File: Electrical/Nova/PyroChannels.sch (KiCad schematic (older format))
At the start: 2 parts

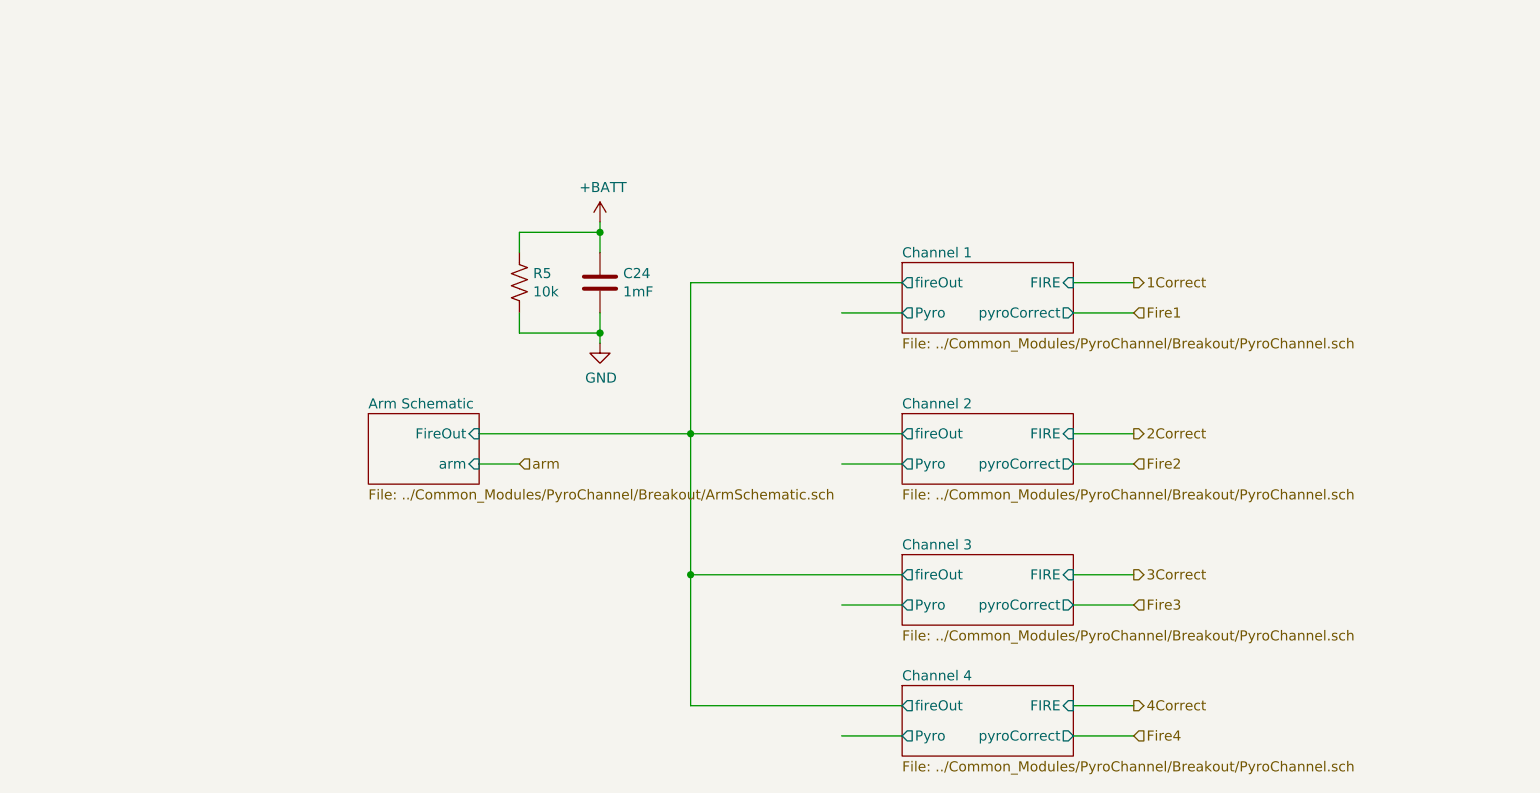
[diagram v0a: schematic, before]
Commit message: More Pin Additions for connectors and other misc.
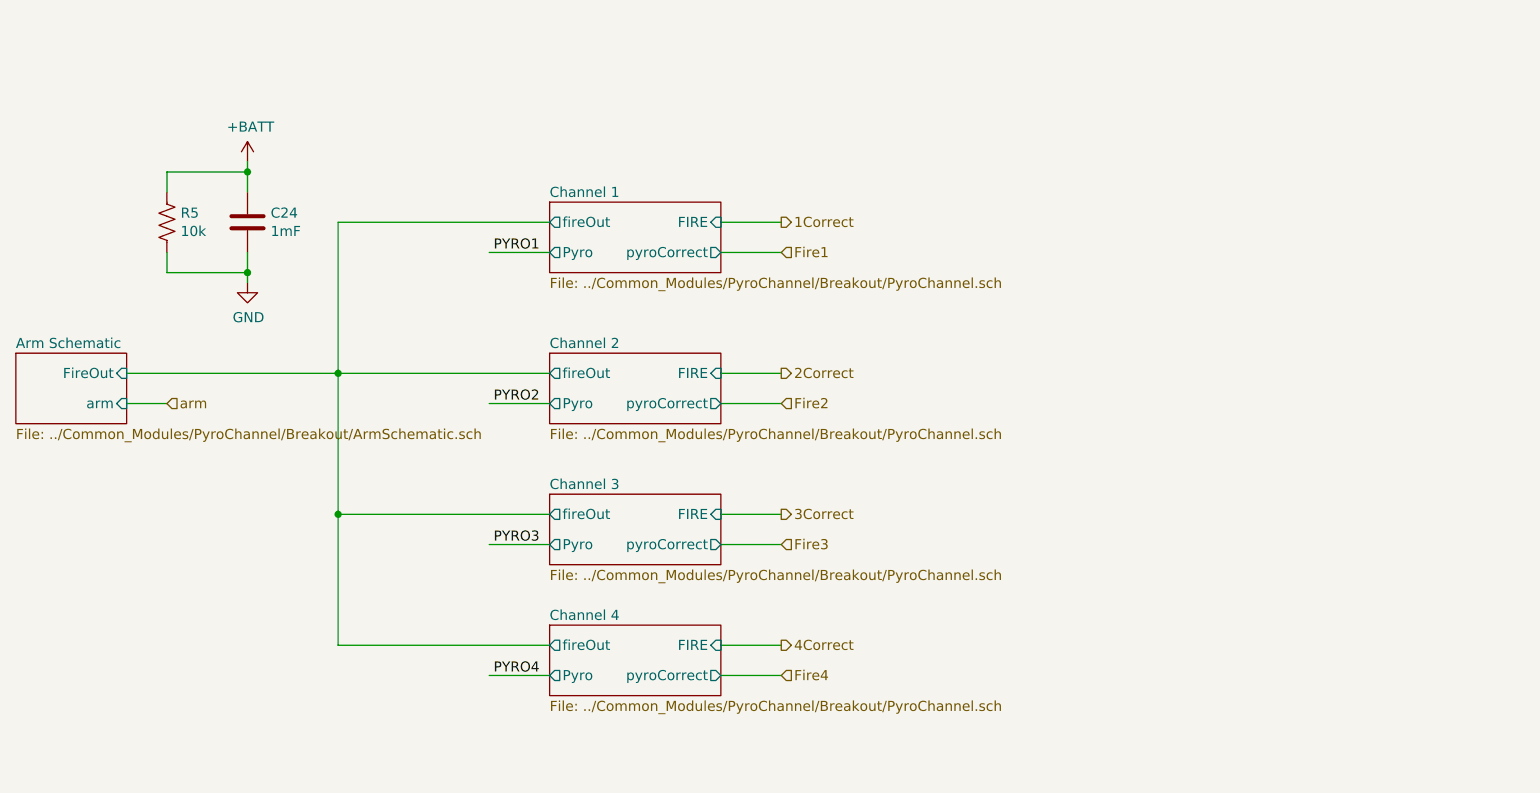
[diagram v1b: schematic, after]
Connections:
- net labels added: PYRO1, PYRO2, PYRO3, PYRO4
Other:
- moved on the sheet: C24, R5
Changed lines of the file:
@@
 $Descr USLetter 11000 8500
 encoding utf-8
-Sheet 12 21
+Sheet 10 21
 Title ""
 Date ""
@@
 L Device:C C24
 U 1 1 5F4497A2
-P 4450 3450
-F 0 "C24" H 4565 3496 50  0000 L CNN
-F 1 "1mF" H 4565 3405 50  0000 L CNN
-F 2 "" H 4488 3300 50  0001 C CNN
-F 3 "~" H 4450 3450 50  0001 C CNN
-F 4 "1189-3703-1-ND" H 4450 3450 50  0001 C CNN "digikey"
-	1    4450 3450
+P 2700 3150
+F 0 "C24" H 2815 3196 50  0000 L CNN
+F 1 "1mF" H 2815 3105 50  0000 L CNN
+F 2 "" H 2738 3000 50  0001 C CNN
+F 3 "~" H 2700 3150 50  0001 C CNN
+F 4 "1189-3703-1-ND" H 2700 3150 50  0001 C CNN "digikey"
+	1    2700 3150
 	1    0    0    -1
 $EndComp
@@
 L power:+BATT #PWR035
 U 1 1 5F449DDB
-P 4450 3150
-F 0 "#PWR035" H 4450 3000 50  0001 C CNN
-F 1 "+BATT" H 4465 3323 50  0000 C CNN
-F 2 "" H 4450 3150 50  0001 C CNN
-F 3 "" H 4450 3150 50  0001 C CNN
-	1    4450 3150
+P 2700 2850
+F 0 "#PWR035" H 2700 2700 50  0001 C CNN
+F 1 "+BATT" H 2715 3023 50  0000 C CNN
+F 2 "" H 2700 2850 50  0001 C CNN
+F 3 "" H 2700 2850 50  0001 C CNN
+	1    2700 2850
 	1    0    0    -1
 $EndComp
 Wire Wire Line
-	4450 3150 4450 3200
+	2700 2850 2700 2900
 $Comp
 L power:GND #PWR036
 U 1 1 5F44A4A7
-P 4450 3750
-F 0 "#PWR036" H 4450 3500 50  0001 C CNN
-F 1 "GND" H 4455 3577 50  0000 C CNN
-F 2 "" H 4450 3750 50  0001 C CNN
-F 3 "" H 4450 3750 50  0001 C CNN
-	1    4450 3750
+P 2700 3450
+F 0 "#PWR036" H 2700 3200 50  0001 C CNN
+F 1 "GND" H 2705 3277 50  0000 C CNN
+F 2 "" H 2700 3450 50  0001 C CNN
+F 3 "" H 2700 3450 50  0001 C CNN
+	1    2700 3450
 	1    0    0    -1
 $EndComp
 Wire Wire Line
-	4450 3600 4450 3700
+	2700 3300 2700 3400
 Wire Wire Line
-	4050 3600 4050 3700
+	2300 3300 2300 3400
 Wire Wire Line
-	4050 3700 4450 3700
-Connection ~ 4450 3700
+	2300 3400 2700 3400
+Connection ~ 2700 3400
 Wire Wire Line
-	4450 3700 4450 3750
+	2700 3400 2700 3450
 Wire Wire Line
-	4050 3300 4050 3200
+	2300 3000 2300 2900
 Wire Wire Line
-	4050 3200 4450 3200
-Connection ~ 4450 3200
+	2300 2900 2700 2900
+Connection ~ 2700 2900
 Wire Wire Line
-	4450 3200 4450 3300
+	2700 2900 2700 3000
 $Comp
 L Device:R_US R5
 U 1 1 5F6ECA83
-P 4050 3450
-F 0 "R5" H 4118 3496 50  0000 L CNN
-F 1 "10k" H 4118 3405 50  0000 L CNN
-F 2 "Resistor_SMD:R_0402_1005Metric" V 4090 3440 50  0001 C CNN
-F 3 "~" H 4050 3450 50  0001 C CNN
-	1    4050 3450
+P 2300 3150
+F 0 "R5" H 2368 3196 50  0000 L CNN
+F 1 "10k" H 2368 3105 50  0000 L CNN
+F 2 "Resistor_SMD:R_0402_1005Metric" V 2340 3140 50  0001 C CNN
+F 3 "~" H 2300 3150 50  0001 C CNN
+	1    2300 3150
 	1    0    0    -1
 $EndComp
-Text HLabel 7100 5050 2    50   Input ~ 0
+Text HLabel 5350 4750 2    50   Input ~ 0
 Fire3
-Text HLabel 7100 4900 2    50   Output ~ 0
+Text HLabel 5350 4600 2    50   Output ~ 0
 3Correct
 $Sheet
-S 5950 4800 850  350
+S 4200 4500 850  350
 U 5F71312E
 F0 "Channel 3" 50
 F1 "../Common_Modules/PyroChannel/Breakout/PyroChannel.sch" 50
-F2 "FIRE" I R 6800 4900 50
-F3 "pyroCorrect" O R 6800 5050 50
-F4 "fireOut" O L 5950 4900 50
-F5 "Pyro" O L 5950 5050 50
+F2 "FIRE" I R 5050 4600 50
+F3 "pyroCorrect" O R 5050 4750 50
+F4 "fireOut" O L 4200 4600 50
+F5 "Pyro" O L 4200 4750 50
 $EndSheet
 Wire Wire Line
-	7100 5050 6800 5050
+	5350 4750 5050 4750
 Wire Wire Line
-	6800 4900 7100 4900
+	5050 4600 5350 4600
 Wire Wire Line
-	5950 4200 4900 4200
+	4200 3900 3150 3900
 Wire Wire Line
-	5950 3450 4900 3450
+	4200 3150 3150 3150
 Wire Wire Line
-	4900 3450 4900 4200
-Connection ~ 4900 4200
+	3150 3150 3150 3900
+Connection ~ 3150 3900
 Wire Wire Line
-	4900 4200 3850 4200
+	3150 3900 2100 3900
 Wire Wire Line
-	4900 4200 4900 4900
+	3150 3900 3150 4600
 Wire Wire Line
-	4900 4900 5950 4900
-Text HLabel 4050 4350 2    50   Input ~ 0
+	3150 4600 4200 4600
+Text HLabel 2300 4050 2    50   Input ~ 0
 arm
 Wire Wire Line
-	3850 4350 4050 4350
-Text HLabel 7100 4200 2    50   Output ~ 0
+	2100 4050 2300 4050
+Text HLabel 5350 3900 2    50   Output ~ 0
 2Correct
-Text HLabel 7100 4350 2    50   Input ~ 0
+Text HLabel 5350 4050 2    50   Input ~ 0
 Fire2
 Wire Wire Line
-	7100 4350 6800 4350
+	5350 4050 5050 4050
 Wire Wire Line
-	7100 4200 6800 4200
+	5350 3900 5050 3900
 $Sheet
-S 5950 4100 850  350
+S 4200 3800 850  350
 U 5F449170
 F0 "Channel 2" 50
 F1 "../Common_Modules/PyroChannel/Breakout/PyroChannel.sch" 50
-F2 "FIRE" I R 6800 4200 50
-F3 "pyroCorrect" O R 6800 4350 50
-F4 "fireOut" O L 5950 4200 50
-F5 "Pyro" O L 5950 4350 50
+F2 "FIRE" I R 5050 3900 50
+F3 "pyroCorrect" O R 5050 4050 50
+F4 "fireOut" O L 4200 3900 50
+F5 "Pyro" O L 4200 4050 50
 $EndSheet
-Text HLabel 7100 3600 2    50   Input ~ 0
+Text HLabel 5350 3300 2    50   Input ~ 0
 Fire1
 Wire Wire Line
-	7100 3600 6800 3600
+	5350 3300 5050 3300
 Wire Wire Line
-	7100 3450 6800 3450
-Text HLabel 7100 3450 2    50   Output ~ 0
+	5350 3150 5050 3150
+Text HLabel 5350 3150 2    50   Output ~ 0
 1Correct
 $Sheet
-S 5950 3350 850  350
+S 4200 3050 850  350
 U 5F44909A
 F0 "Channel 1" 50
 F1 "../Common_Modules/PyroChannel/Breakout/PyroChannel.sch" 50
-F2 "FIRE" I R 6800 3450 50
-F3 "pyroCorrect" O R 6800 3600 50
-F4 "fireOut" O L 5950 3450 50
-F5 "Pyro" O L 5950 3600 50
+F2 "FIRE" I R 5050 3150 50
+F3 "pyroCorrect" O R 5050 3300 50
+F4 "fireOut" O L 4200 3150 50
+F5 "Pyro" O L 4200 3300 50
 $EndSheet
 Wire Wire Line
-	5950 3600 5650 3600
+	4200 3300 3900 3300
 Wire Wire Line
-	5950 4350 5650 4350
+	4200 4050 3900 4050
 Wire Wire Line
-	5950 5050 5650 5050
+	4200 4750 3900 4750
 $Sheet
-S 3300 4100 550  350
+S 1550 3800 550  350
 U 5F448D89
 F0 "Arm Schematic" 50
 F1 "../Common_Modules/PyroChannel/Breakout/ArmSchematic.sch" 50
-F2 "FireOut" I R 3850 4200 50
-F3 "arm" I R 3850 4350 50
+F2 "FireOut" I R 2100 3900 50
+F3 "arm" I R 2100 4050 50
 $EndSheet
-Text HLabel 7100 5700 2    50   Input ~ 0
+Text HLabel 5350 5400 2    50   Input ~ 0
 Fire4
 Wire Wire Line
-	7100 5700 6800 5700
+	5350 5400 5050 5400
 Wire Wire Line
-	7100 5550 6800 5550
-Text HLabel 7100 5550 2    50   Output ~ 0
+	5350 5250 5050 5250
+Text HLabel 5350 5250 2    50   Output ~ 0
 4Correct
 $Sheet
-S 5950 5450 850  350
+S 4200 5150 850  350
 U 6040FF20
 F0 "Channel 4" 50
 F1 "../Common_Modules/PyroChannel/Breakout/PyroChannel.sch" 50
-F2 "FIRE" I R 6800 5550 50
-F3 "pyroCorrect" O R 6800 5700 50
-F4 "fireOut" O L 5950 5550 50
-F5 "Pyro" O L 5950 5700 50
+F2 "FIRE" I R 5050 5250 50
+F3 "pyroCorrect" O R 5050 5400 50
+F4 "fireOut" O L 4200 5250 50
+F5 "Pyro" O L 4200 5400 50
 $EndSheet
 Wire Wire Line
-	5950 5700 5650 5700
+	4200 5400 3900 5400
 Wire Wire Line
-	4900 5550 5950 5550
+	3150 5250 4200 5250
 Wire Wire Line
-	4900 4900 4900 5550
-Connection ~ 4900 4900
+	3150 4600 3150 5250
+Connection ~ 3150 4600
+Text Label 4150 3300 2    50   ~ 0
+PYRO1
+Text Label 4150 4050 2    50   ~ 0
+PYRO2
+Text Label 4150 4750 2    50   ~ 0
+PYRO3
+Text Label 4150 5400 2    50   ~ 0
+PYRO4
 $EndSCHEMATC

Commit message: Added Pyro Connectors and removed unneeded decoupling caps
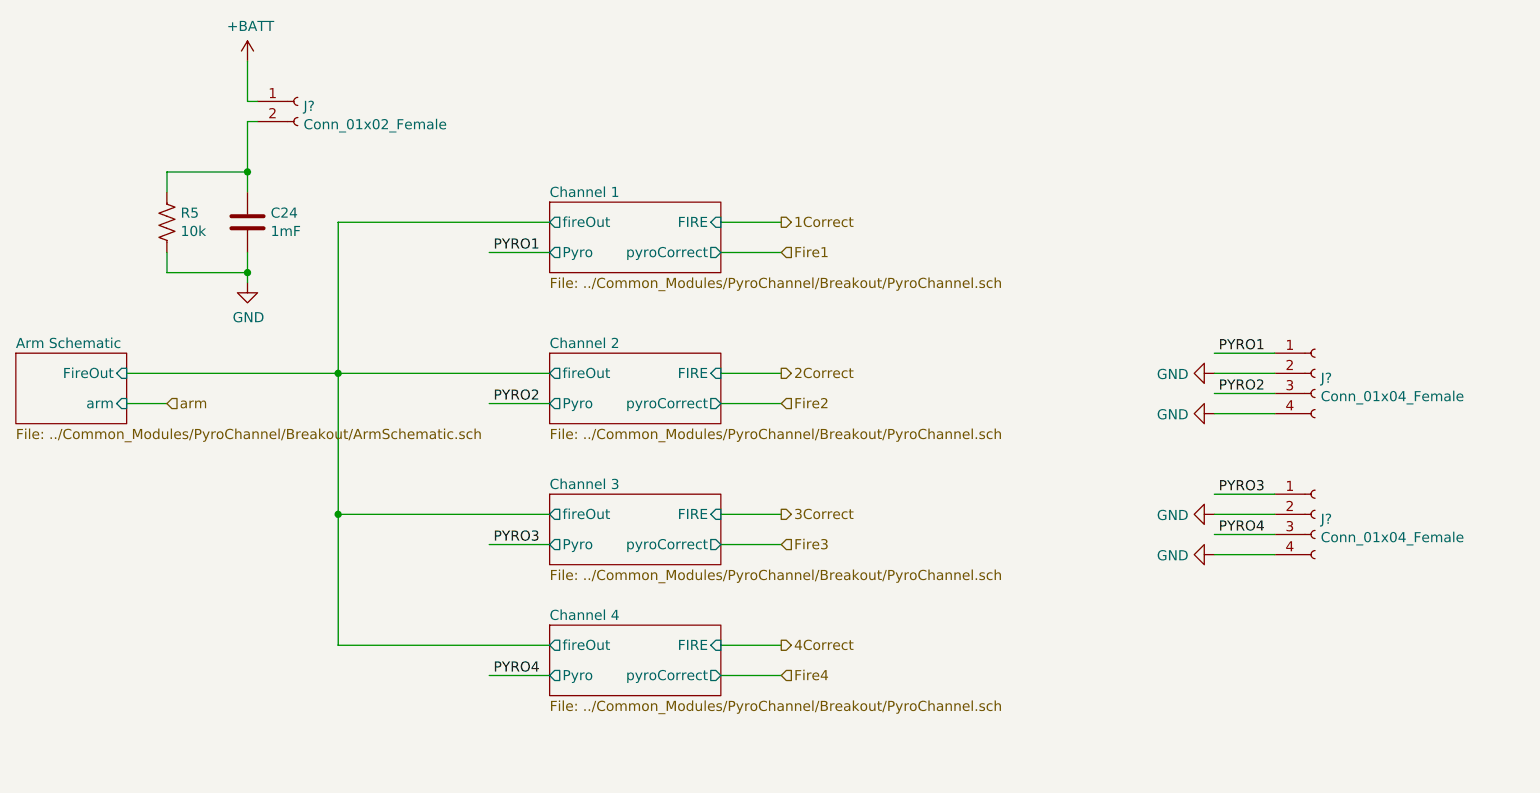
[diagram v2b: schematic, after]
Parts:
- added J? (x2): Conn_01x04_Female, symbol Connector:Conn_01x04_Female
- added J?: Conn_01x02_Female, symbol Connector:Conn_01x02_Female
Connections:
- wire segments 29 -> 40
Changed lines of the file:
@@
 L power:+BATT #PWR035
 U 1 1 5F449DDB
-P 2700 2850
-F 0 "#PWR035" H 2700 2700 50  0001 C CNN
-F 1 "+BATT" H 2715 3023 50  0000 C CNN
-F 2 "" H 2700 2850 50  0001 C CNN
-F 3 "" H 2700 2850 50  0001 C CNN
-	1    2700 2850
-	1    0    0    -1
-$EndComp
-Wire Wire Line
-	2700 2850 2700 2900
+P 2700 2350
+F 0 "#PWR035" H 2700 2200 50  0001 C CNN
+F 1 "+BATT" H 2715 2523 50  0000 C CNN
+F 2 "" H 2700 2350 50  0001 C CNN
+F 3 "" H 2700 2350 50  0001 C CNN
+	1    2700 2350
+	1    0    0    -1
+$EndComp
 $Comp
 L power:GND #PWR036
@@
 Text Label 4150 5400 2    50   ~ 0
 PYRO4
+$Comp
+L Connector:Conn_01x04_Female J?
+U 1 1 6033E472
+P 8000 3900
+F 0 "J?" H 8028 3876 50  0000 L CNN
+F 1 "Conn_01x04_Female" H 8028 3785 50  0000 L CNN
+F 2 "" H 8000 3900 50  0001 C CNN
+F 3 "~" H 8000 3900 50  0001 C CNN
+	1    8000 3900
+	1    0    0    -1
+$EndComp
+$Comp
+L Connector:Conn_01x04_Female J?
+U 1 1 6033EDCD
+P 8000 4600
+F 0 "J?" H 8028 4576 50  0000 L CNN
+F 1 "Conn_01x04_Female" H 8028 4485 50  0000 L CNN
+F 2 "" H 8000 4600 50  0001 C CNN
+F 3 "~" H 8000 4600 50  0001 C CNN
+	1    8000 4600
+	1    0    0    -1
+$EndComp
+Wire Wire Line
+	7800 3800 7500 3800
+Text Label 7750 3800 2    50   ~ 0
+PYRO1
+Wire Wire Line
+	7800 4000 7500 4000
+Text Label 7750 4000 2    50   ~ 0
+PYRO2
+Wire Wire Line
+	7800 4500 7500 4500
+Text Label 7750 4500 2    50   ~ 0
+PYRO3
+Wire Wire Line
+	7800 4700 7500 4700
+Text Label 7750 4700 2    50   ~ 0
+PYRO4
+$Comp
+L power:GND #PWR?
+U 1 1 60342F05
+P 7500 3900
+F 0 "#PWR?" H 7500 3650 50  0001 C CNN
+F 1 "GND" V 7505 3772 50  0000 R CNN
+F 2 "" H 7500 3900 50  0001 C CNN
+F 3 "" H 7500 3900 50  0001 C CNN
+	1    7500 3900
+	0    1    1    0
+$EndComp
+$Comp
+L power:GND #PWR?
+U 1 1 603438C3
+P 7500 4100
+F 0 "#PWR?" H 7500 3850 50  0001 C CNN
+F 1 "GND" V 7505 3972 50  0000 R CNN
+F 2 "" H 7500 4100 50  0001 C CNN
+F 3 "" H 7500 4100 50  0001 C CNN
+	1    7500 4100
+	0    1    1    0
+$EndComp
+$Comp
+L power:GND #PWR?
+U 1 1 60343E90
+P 7500 4600
+F 0 "#PWR?" H 7500 4350 50  0001 C CNN
+F 1 "GND" V 7505 4472 50  0000 R CNN
+F 2 "" H 7500 4600 50  0001 C CNN
+F 3 "" H 7500 4600 50  0001 C CNN
+	1    7500 4600
+	0    1    1    0
+$EndComp
+$Comp
+L power:GND #PWR?
+U 1 1 603444B0
+P 7500 4800
+F 0 "#PWR?" H 7500 4550 50  0001 C CNN
+F 1 "GND" V 7505 4672 50  0000 R CNN
+F 2 "" H 7500 4800 50  0001 C CNN
+F 3 "" H 7500 4800 50  0001 C CNN
+	1    7500 4800
+	0    1    1    0
+$EndComp
+Wire Wire Line
+	7800 4800 7500 4800
+Wire Wire Line
+	7500 4600 7800 4600
+Wire Wire Line
+	7800 4100 7500 4100
+Wire Wire Line
+	7500 3900 7800 3900
+$Comp
+L Connector:Conn_01x02_Female J?
+U 1 1 60348F4E
+P 2950 2550
+F 0 "J?" H 2978 2526 50  0000 L CNN
+F 1 "Conn_01x02_Female" H 2978 2435 50  0000 L CNN
+F 2 "" H 2950 2550 50  0001 C CNN
+F 3 "~" H 2950 2550 50  0001 C CNN
+	1    2950 2550
+	1    0    0    -1
+$EndComp
+Wire Wire Line
+	2700 2350 2700 2550
+Wire Wire Line
+	2700 2550 2750 2550
+Wire Wire Line
+	2750 2650 2700 2650
+Wire Wire Line
+	2700 2650 2700 2900
 $EndSCHEMATC

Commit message: Added a bunch of footprints to symbols
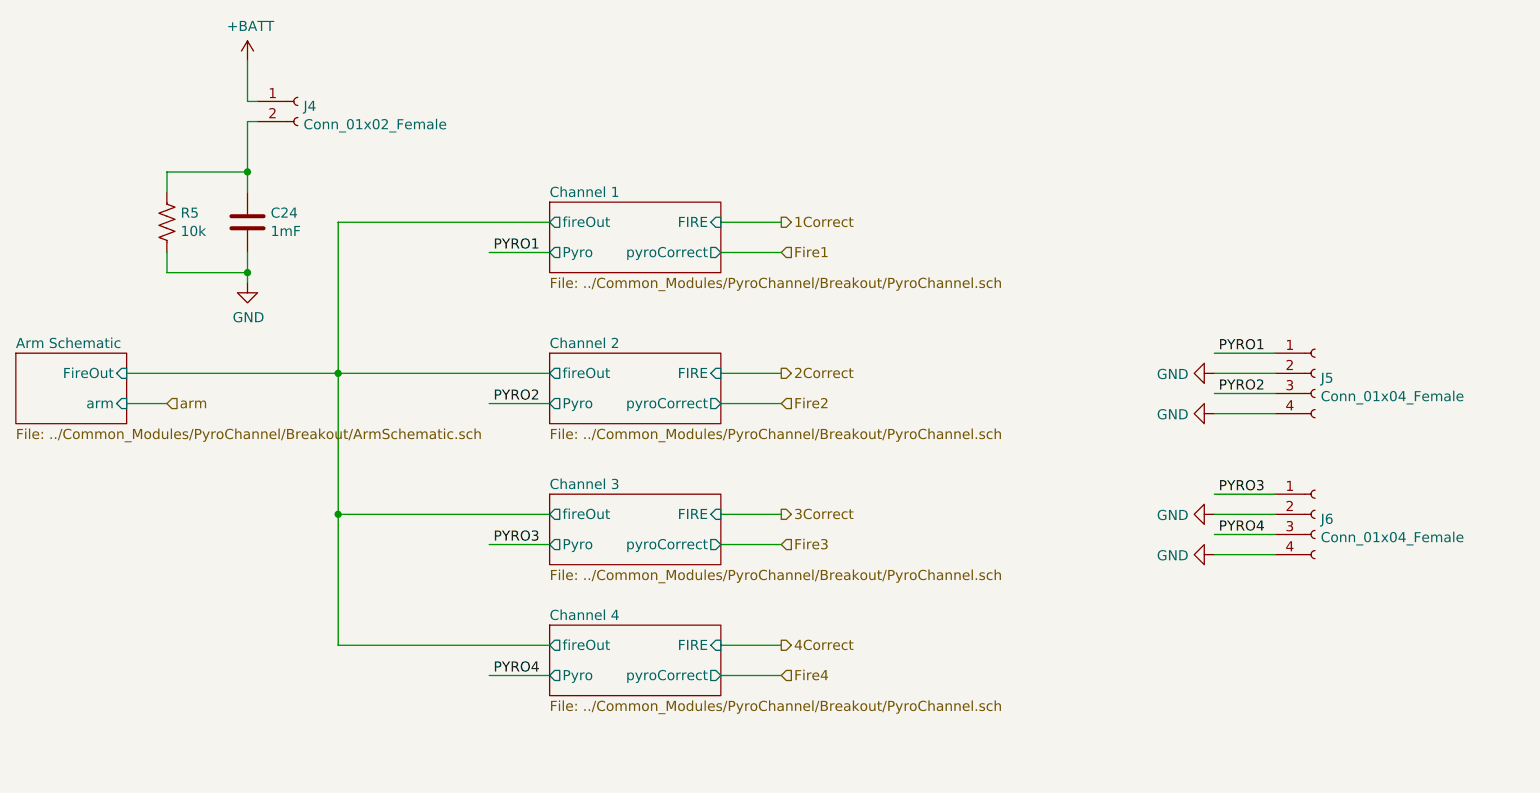
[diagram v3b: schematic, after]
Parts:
- C24: footprint (none) -> PyroChannel:CP_Radial_D10.0mm_P5.00mm
- gave numbers to parts that had none: 3
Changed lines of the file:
@@
 F 0 "C24" H 2815 3196 50  0000 L CNN
 F 1 "1mF" H 2815 3105 50  0000 L CNN
-F 2 "" H 2738 3000 50  0001 C CNN
+F 2 "PyroChannel:CP_Radial_D10.0mm_P5.00mm" H 2738 3000 50  0001 C CNN
 F 3 "~" H 2700 3150 50  0001 C CNN
 F 4 "1189-3703-1-ND" H 2700 3150 50  0001 C CNN "digikey"
@@
 PYRO4
 $Comp
-L Connector:Conn_01x04_Female J?
+L Connector:Conn_01x04_Female J5
 U 1 1 6033E472
 P 8000 3900
-F 0 "J?" H 8028 3876 50  0000 L CNN
+F 0 "J5" H 8028 3876 50  0000 L CNN
 F 1 "Conn_01x04_Female" H 8028 3785 50  0000 L CNN
 F 2 "" H 8000 3900 50  0001 C CNN
@@
 $EndComp
 $Comp
-L Connector:Conn_01x04_Female J?
+L Connector:Conn_01x04_Female J6
 U 1 1 6033EDCD
 P 8000 4600
-F 0 "J?" H 8028 4576 50  0000 L CNN
+F 0 "J6" H 8028 4576 50  0000 L CNN
 F 1 "Conn_01x04_Female" H 8028 4485 50  0000 L CNN
 F 2 "" H 8000 4600 50  0001 C CNN
@@
 PYRO4
 $Comp
-L power:GND #PWR?
+L power:GND #PWR0128
 U 1 1 60342F05
 P 7500 3900
-F 0 "#PWR?" H 7500 3650 50  0001 C CNN
+F 0 "#PWR0128" H 7500 3650 50  0001 C CNN
 F 1 "GND" V 7505 3772 50  0000 R CNN
 F 2 "" H 7500 3900 50  0001 C CNN
@@
 $EndComp
 $Comp
-L power:GND #PWR?
+L power:GND #PWR0129
 U 1 1 603438C3
 P 7500 4100
-F 0 "#PWR?" H 7500 3850 50  0001 C CNN
+F 0 "#PWR0129" H 7500 3850 50  0001 C CNN
 F 1 "GND" V 7505 3972 50  0000 R CNN
 F 2 "" H 7500 4100 50  0001 C CNN
@@
 $EndComp
 $Comp
-L power:GND #PWR?
+L power:GND #PWR0130
 U 1 1 60343E90
 P 7500 4600
-F 0 "#PWR?" H 7500 4350 50  0001 C CNN
+F 0 "#PWR0130" H 7500 4350 50  0001 C CNN
 F 1 "GND" V 7505 4472 50  0000 R CNN
 F 2 "" H 7500 4600 50  0001 C CNN
@@
 $EndComp
 $Comp
-L power:GND #PWR?
+L power:GND #PWR0131
 U 1 1 603444B0
 P 7500 4800
-F 0 "#PWR?" H 7500 4550 50  0001 C CNN
+F 0 "#PWR0131" H 7500 4550 50  0001 C CNN
 F 1 "GND" V 7505 4672 50  0000 R CNN
 F 2 "" H 7500 4800 50  0001 C CNN
@@
 	7500 3900 7800 3900
 $Comp
-L Connector:Conn_01x02_Female J?
+L Connector:Conn_01x02_Female J4
 U 1 1 60348F4E
 P 2950 2550
-F 0 "J?" H 2978 2526 50  0000 L CNN
+F 0 "J4" H 2978 2526 50  0000 L CNN
 F 1 "Conn_01x02_Female" H 2978 2435 50  0000 L CNN
 F 2 "" H 2950 2550 50  0001 C CNN
